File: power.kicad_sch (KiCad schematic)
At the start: 19 parts, among them J9 Conn_01x02, U5 LDL212PV33R, U9 TPS62933

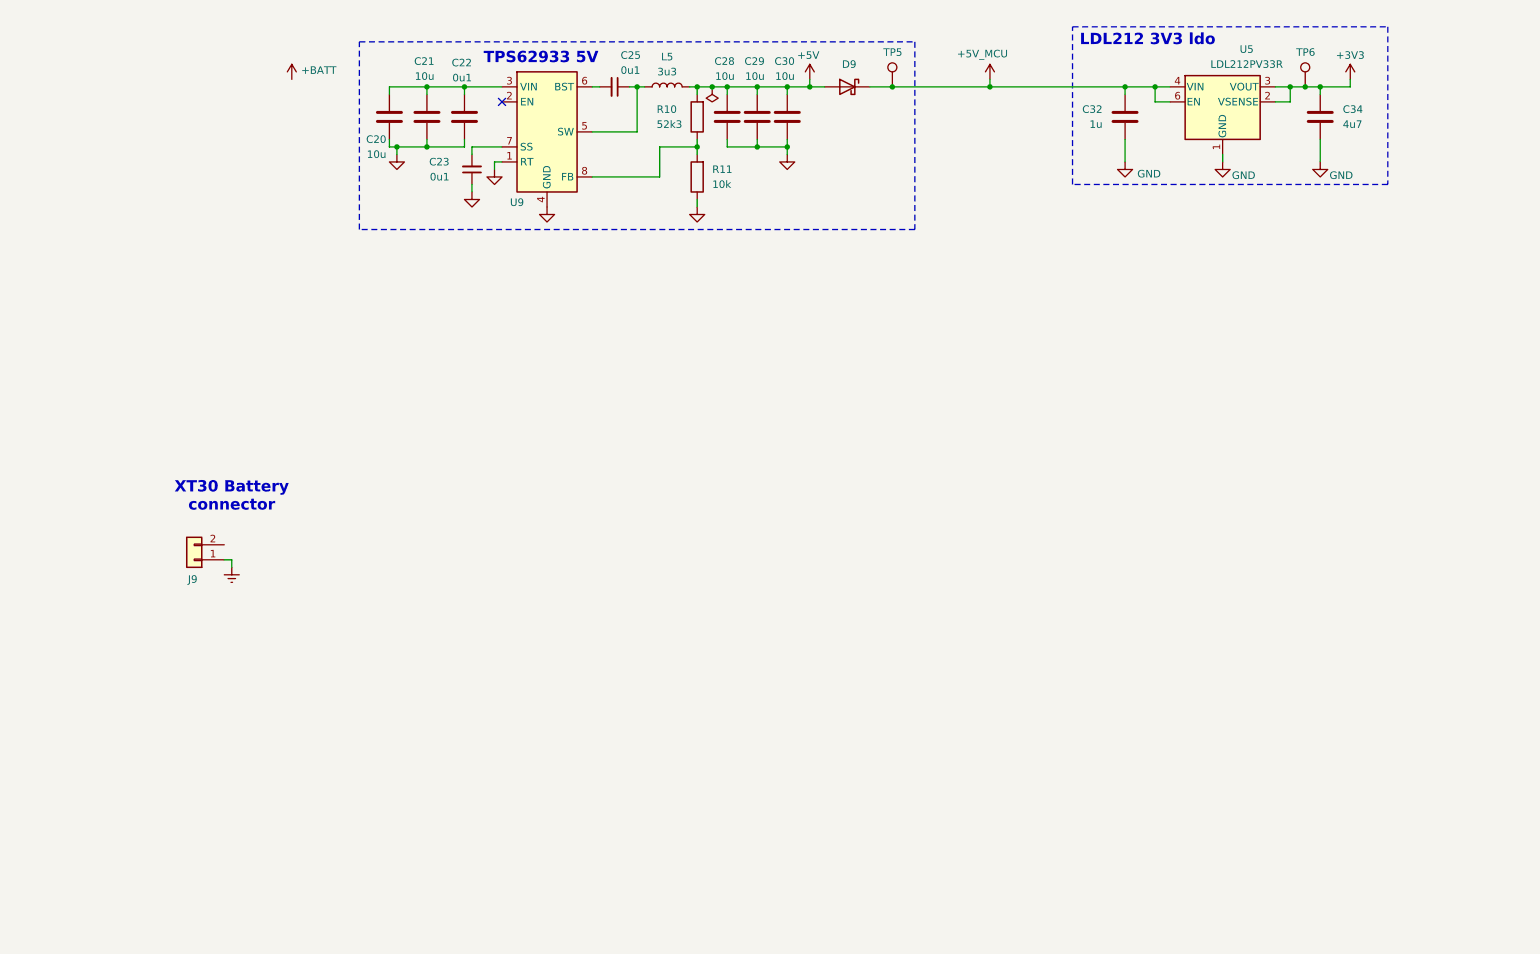
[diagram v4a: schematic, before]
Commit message: schem: add BQ25798 MPPT/Charger/Protection/Boost
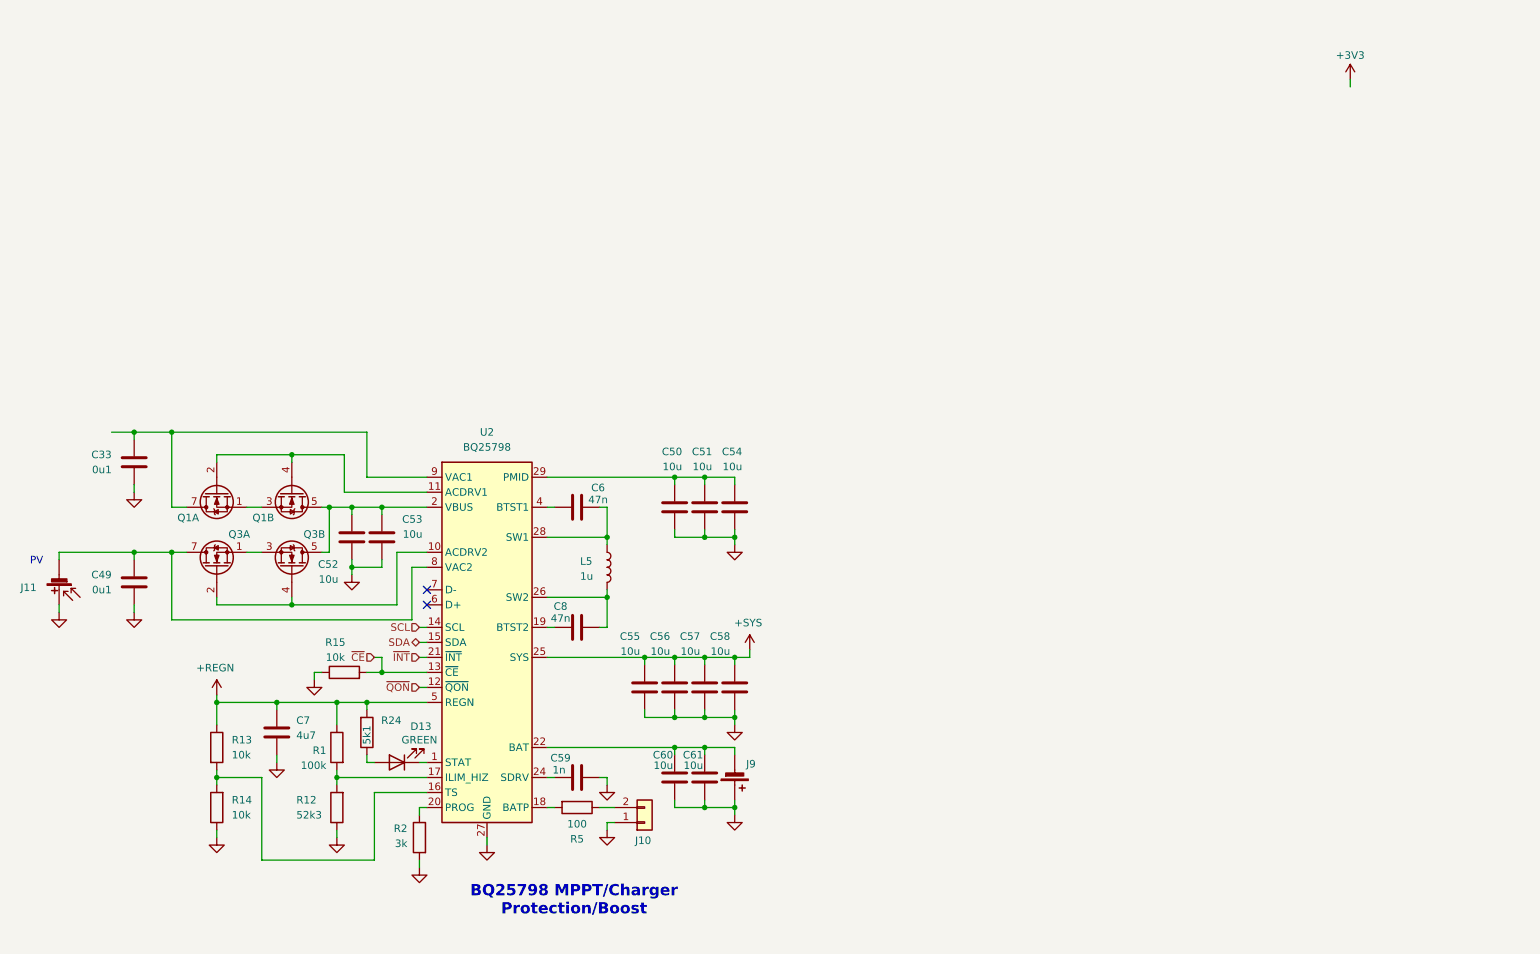
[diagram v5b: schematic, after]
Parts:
- removed C20, C21, C28, C29, C30: 10u, Capacitor_SMD:C_0805_2012Metric, symbol Device:C
- removed C22: 0u1, Capacitor_SMD:C_0402_1005Metric, symbol Device:C
- removed C23, C25: 0u1, Capacitor_SMD:C_0402_1005Metric, symbol Device:C_Small
- removed C32: 1u, Capacitor_SMD:C_0402_1005Metric, symbol Device:C
- removed C34: 4u7, Capacitor_SMD:C_0402_1005Metric, symbol Device:C
- removed D9: D_Schottky, Diode_SMD:D_SMA, symbol Device:D_Schottky
- removed J9: Conn_01x02, Connector_AMASS:AMASS_XT30PW-M_1x02_P2.50mm_Horizontal, symbol Connector_Generic:Conn_01x02
- removed R10: 52k3, Resistor_SMD:R_0402_1005Metric, symbol Device:R
- removed R11: 10k, Resistor_SMD:R_0402_1005Metric, symbol Device:R
- removed TP5, TP6: TestPoint, TestPoint:TestPoint_Pad_D2.0mm, symbol Connector:TestPoint
- removed U5: LDL212PV33R, GLCS:DFN-6-1EP_2x2mm_P0.5mm_ST, symbol GLCS:LDL212PV33R
- removed U9: TPS62933, Package_TO_SOT_SMD:SOT-583-8, symbol Regulator_Switching:TPS62933
- added C33, C49: 0u1, Capacitor_SMD:C_0402_1005Metric, symbol Device:C
- added C50, C51, C52, C53, C54, C55, C56, C57, C58, C60, C61: 10u, Capacitor_SMD:C_0805_2012Metric, symbol Device:C
- added C59: 1n, Capacitor_SMD:C_0402_1005Metric, symbol Device:C
- added C6, C8: 47n, symbol Device:C
- added C7: 4u7, symbol Device:C
- added D13: GREEN, LED_SMD:LED_0805_2012Metric, symbol Device:LED
- added J10: Conn_01x02, Connector_JST:JST_XH_B2B-XH-A_1x02_P2.50mm_Vertical, symbol Connector_Generic:Conn_01x02
- added J11: Solar_Cell, Connector_JST:JST_XH_B2B-XH-A_1x02_P2.50mm_Vertical, symbol Device:Solar_Cell
- added J9: Battery_Cell, Connector_AMASS:AMASS_XT30PW-M_1x02_P2.50mm_Horizontal, symbol Device:Battery_Cell
- added Q1, Q3: AO4882, Package_SO:SOIC-8_3.9x4.9mm_P1.27mm, symbol Transistor_FET:AO4842
- added R1: 100k, symbol Device:R
- added R12: 52k3, Resistor_SMD:R_0402_1005Metric, symbol Device:R
- added R13, R14, R15: 10k, Resistor_SMD:R_0402_1005Metric, symbol Device:R
- added R2: 3k, symbol Device:R
- added R24: 5k1, Resistor_SMD:R_0402_1005Metric, symbol Device:R
- added R5: 100, symbol Device:R
- added U2: BQ25798, Package_DFN_QFN:Texas_RQM0029A_VQFN-29_4x4mm_P0.4mm, symbol Battery_Management:BQ25798
- L5: value 3u3 -> 1u; footprint Inductor_SMD:L_Sunlord_MWSA0402S -> (none); Basic X -> (none); JLCPCB Part # C167207 -> (none); Manufacturer cjiang -> (none); Manufacturer Part Number FXL0420-3R3-M -> (none)
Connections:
- net GND: now also C33.2, C49.2, C50.2, C51.2, C52.2, C53.2, C54.2, C55.2, C56.2, C57.2, C58.2, C59.2, C60.2, C61.2, C7.2, J10.1 (Pin_1), J11.1 (+), J9.1 (+), R12.1, R14.1, R15.1, R2.2, U2.27 (GND)
- net at L5.1: now also C6.2, U2.28 (SW1)
- net +5V: no longer names the net of L5.2
- net +5V: now also C8.2, U2.26 (SW2)
- new net: C50.1, C51.1, C54.1, U2.29 (PMID)
- new net: J10.2 (Pin_2), R5.1
- new net: D13.2 (A), R24.1
- new net: C8.1, U2.19 (BTST2)
- new net: C59.1, U2.24 (SDRV)
- new net: R1.2, R12.2, U2.17 (ILIM_HIZ)
- new net: R2.1, U2.20 (PROG)
- new net: D13.1 (K), U2.1 (STAT)
- new net: Q3.2 (G1), Q3.4 (G2), U2.10 (ACDRV2)
- new net: Q1.2 (G1), Q1.4 (G2), U2.11 (ACDRV1)
- new net: R13.2, R14.2, U2.16 (TS)
- new net: R5.2, U2.18 (BATP)
- new net: C52.1, C53.1, Q1.5 (D2), Q1.6 (D2), Q3.5 (D2), Q3.6 (D2), U2.2 (VBUS), U2.3 (VBUS)
- new net: C60.1, C61.1, J9.2 (-), U2.22 (BAT), U2.23 (BAT)
- new net: C6.1, U2.4 (BTST1)
- new net: C49.1, J11.2 (-), Q3.7 (D1), Q3.8 (D1), U2.8 (VAC2)
- new net: C33.1, Q1.7 (D1), Q1.8 (D1), U2.9 (VAC1)
- new net: Q3.1 (S1), Q3.3 (S2)
- new net: Q1.1 (S1), Q1.3 (S2)
- new net +REGN: C7.1, R1.1, R13.1, R24.2, U2.5 (REGN)
- new net +SYS: C55.1, C56.1, C57.1, C58.1, U2.25 (SYS)
- new net SCL: U2.14 (SCL)
- new net SDA: U2.15 (SDA)
- new net ~{CE}: R15.2, U2.13 (~{CE})
- new net ~{INT}: U2.21 (~{INT})
- new net ~{QON}: U2.12 (~{QON})
- no-connect marks 1 -> 2
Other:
- note added: "BQ25798 MPPT/Charger Protection/Boost"
- note added: "PV"
- note removed: "LDL212 3V3 ldo"
- note removed: "TPS62933 5V"
- note removed: "XT30 Battery connector"

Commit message: schem: add TPS6282 3.3v SMPS
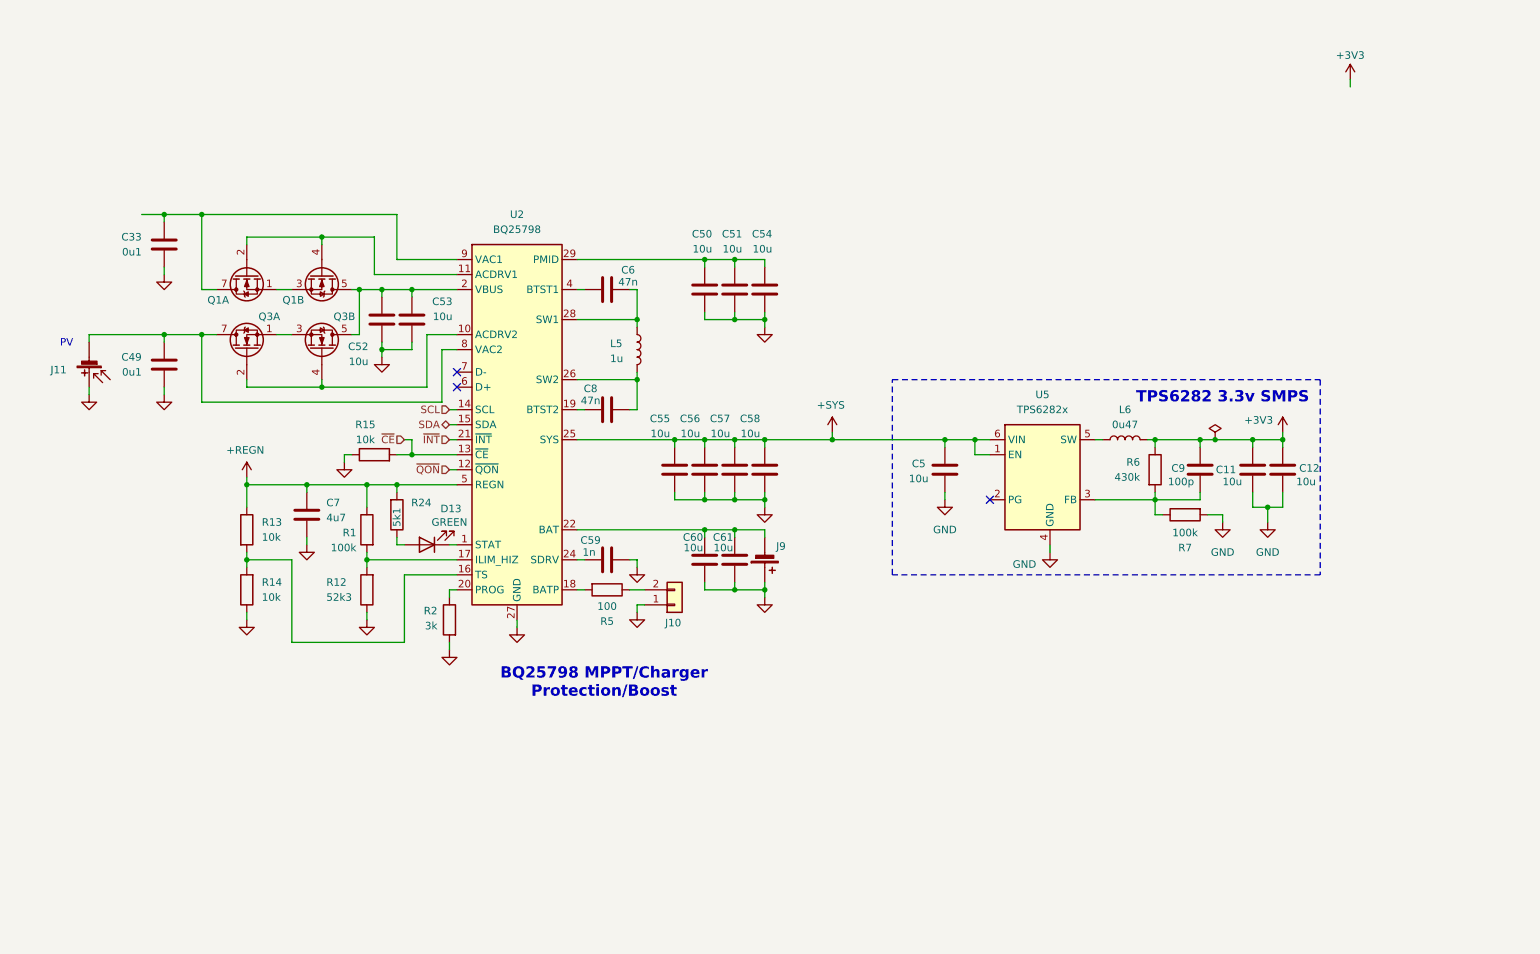
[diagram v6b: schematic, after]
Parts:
- added C11, C12: 10u, Capacitor_SMD:C_0402_1005Metric, symbol Device:C
- added C5: 10u, Capacitor_SMD:C_0603_1608Metric, symbol Device:C
- added C9: 100p, Capacitor_SMD:C_0402_1005Metric, symbol Device:C
- added L6: 0u47, Pers:TDK_TFM201610ALC, symbol Device:L
- added R6: 430k, Resistor_SMD:R_0603_1608Metric, symbol Device:R
- added R7: 100k, Resistor_SMD:R_0402_1005Metric, symbol Device:R
- added U5: TPS6282x, Pers:Texas_VSON-6_1.5x1.5mm_P0.5mm_DMQ0006A, symbol Pers:TPS6282x
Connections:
- net +3V3: now also C11.1, C12.1, C9.1, L6.2, R6.1
- net +SYS: now also C5.1, U5.1 (EN), U5.6 (VIN)
- net GND: now also C11.2, C12.2, C5.2, R7.2, U5.4 (GND)
- new net: C9.2, R6.2, R7.1, U5.3 (FB)
- new net: L6.1, U5.5 (SW)
- no-connect marks 2 -> 3
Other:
- note added: "TPS6282 3.3v SMPS"
- moved on the sheet: C33, C49, C50, C51, C52, C53, C54, C55, C56, C57, C58, C59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

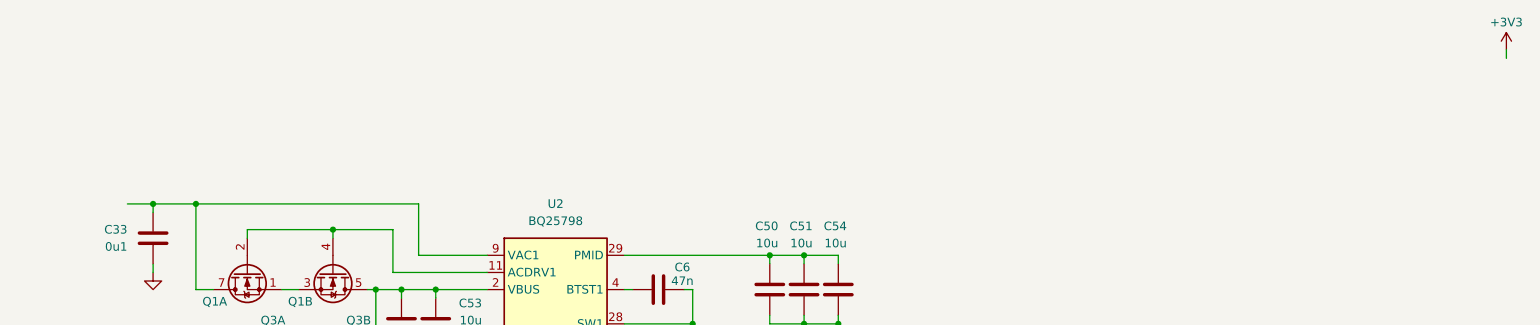
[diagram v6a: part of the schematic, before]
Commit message: schem: remove esp32
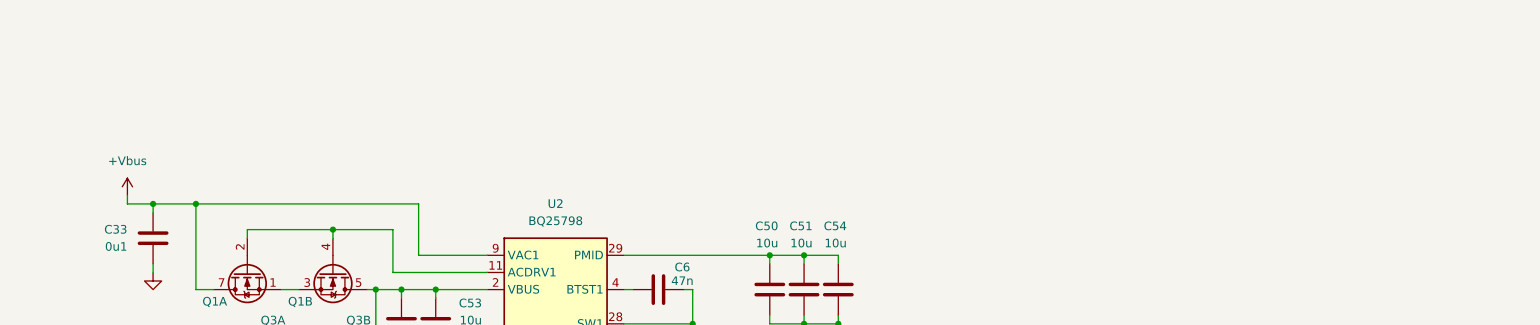
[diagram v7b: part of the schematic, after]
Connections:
- net +Vbus: now reaches C33.1, Q1.7 (D1), Q1.8 (D1), U2.9 (VAC1)
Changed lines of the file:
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@@
 	)
 	(junction
-		(at 45.72 67.31)
-		(diameter 0)
-		(color 0 0 0 0)
-	)
-	(junction
 		(at 232.41 116.84)
 		(diameter 0)
@@
 	)
 	(junction
+		(at 45.72 67.31)
+		(diameter 0)
+		(color 0 0 0 0)
+	)
+	(junction
 		(at 52.07 87.63)
 		(diameter 0)
@@
 	(wire
 		(pts
-			(xy 246.38 44.45) (xy 246.38 45.72)
-		)
-		(stroke
-			(width 0)
-			(type default)
-		)
-	)
-	(wire
-		(pts
 			(xy 125.73 133.35) (xy 125.73 134.62)
 		)
@@
 	(wire
 		(pts
+			(xy 41.91 67.31) (xy 41.91 66.04)
+		)
+		(stroke
+			(width 0)
+			(type default)
+		)
+	)
+	(wire
+		(pts
 			(xy 93.98 100.33) (xy 95.25 100.33)
 		)
@@
 	)
 	(symbol
+		(lib_id "power:VBUS")
+		(at 41.91 66.04 0)
+		(mirror y)
+		(unit 1)
+		(body_style 1)
+		(exclude_from_sim no)
+		(in_bom yes)
+		(on_board yes)
+		(in_pos_files yes)
+		(dnp no)
+		(fields_autoplaced yes)
+		(property "Reference" "#PWR012"
+			(at 41.91 69.85 0)
+			(hide yes)
+			(show_name no)
+			(do_not_autoplace no)
+			(effects
+				(font
+					(size 1.27 1.27)
+				)
+			)
+		)
+		(property "Value" "+Vbus"
+			(at 41.91 60.96 0)
+			(show_name no)
+			(do_not_autoplace no)
+			(effects
+				(font
+					(size 1.27 1.27)
+				)
+			)
+		)
+		(property "Footprint" ""
+			(at 41.91 66.04 0)
+			(hide yes)
+			(show_name no)
+			(do_not_autoplace no)
+			(effects
+				(font
+					(size 1.27 1.27)
+				)
+			)
+		)
+		(property "Datasheet" ""
+			(at 41.91 66.04 0)
+			(hide yes)
+			(show_name no)
+			(do_not_autoplace no)
+			(effects
+				(font
+					(size 1.27 1.27)
+				)
+			)
+		)
+		(property "Description" "Power symbol creates a global label with name \"VBUS\""
+			(at 41.91 66.04 0)
+			(hide yes)
+			(show_name no)
+			(do_not_autoplace no)
+			(effects
+				(font
+					(size 1.27 1.27)
+				)
+			)
+		)
+		(pin "1"
+		)
+		(instances
+			(project "carte-meteo-lora-1"
+				(path "/13f499c2-4dc3-4e2c-8cf4-c7d5e00eb573/b13f5423-ad2b-486f-b3c9-143f0bee9d57"
+					(reference "#PWR012")
+					(unit 1)
+				)
+			)
+		)
+	)
+	(symbol
 		(lib_id "Device:C")
 		(at 147.32 110.49 0)
@@
 					(unit 1)
 				)
-			)
-		)
-	)
-	(symbol
-		(lib_id "power:+3V3")
-		(at 246.38 44.45 0)
-		(unit 1)
-		(body_style 1)
-		(exclude_from_sim no)
-		(in_bom yes)
-		(on_board yes)
-		(in_pos_files yes)
-		(dnp no)
-		(property "Reference" "#PWR075"
-			(at 246.38 48.26 0)
-			(hide yes)
-			(show_name no)
-			(do_not_autoplace no)
-			(effects
-				(font
-					(size 1.27 1.27)
-				)
-			)
-		)
-		(property "Value" "+3V3"
-			(at 246.38 40.386 0)
-			(show_name no)
-			(do_not_autoplace no)
-			(effects
-				(font
-					(size 1.27 1.27)
-				)
-			)
-		)
-		(property "Footprint" ""
-			(at 246.38 44.45 0)
-			(hide yes)
-			(show_name no)
-			(do_not_autoplace no)
-			(effects
-				(font
-					(size 1.27 1.27)
-				)
-			)
-		)
-		(property "Datasheet" ""
-			(at 246.38 44.45 0)
-			(hide yes)
-			(show_name no)
-			(do_not_autoplace no)
-			(effects
-				(font
-					(size 1.27 1.27)
-				)
-			)
-		)
-		(property "Description" "Power symbol creates a global label with name \"+3V3\""
-			(at 246.38 44.45 0)
-			(hide yes)
-			(show_name no)
-			(do_not_autoplace no)
-			(effects
-				(font
-					(size 1.27 1.27)
-				)
-			)
-		)
-		(pin "1"
-		)
-		(instances
-			(project "carte-meteo-lora-1"
-				(path "/13f499c2-4dc3-4e2c-8cf4-c7d5e00eb573/b13f5423-ad2b-486f-b3c9-143f0bee9d57"
-					(reference "#PWR075")
-					(unit 1)
-				)
